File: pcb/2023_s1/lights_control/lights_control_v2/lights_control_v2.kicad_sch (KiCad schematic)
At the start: 9 parts

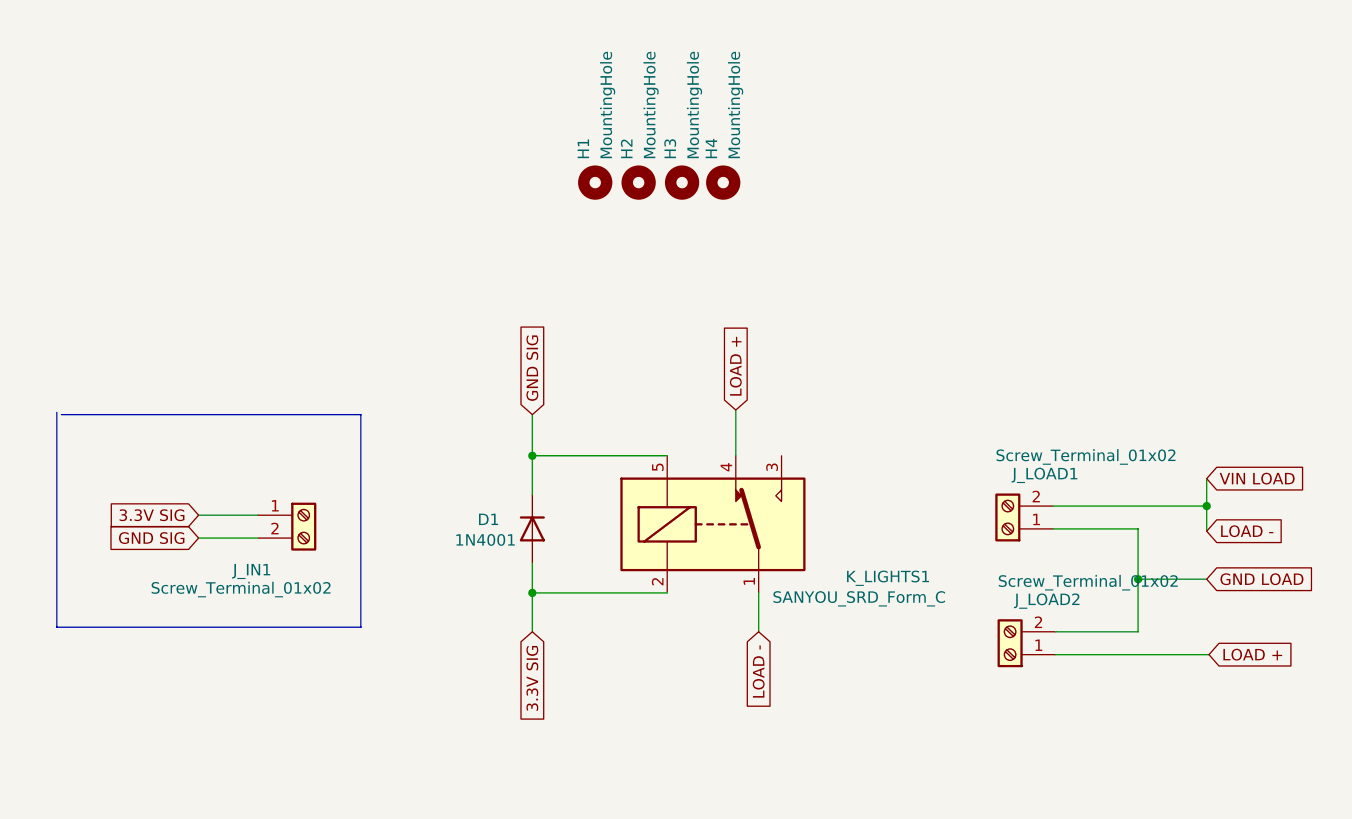
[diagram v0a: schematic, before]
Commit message: fix, forgot to use 2N2222 as current amplifier of the input signal
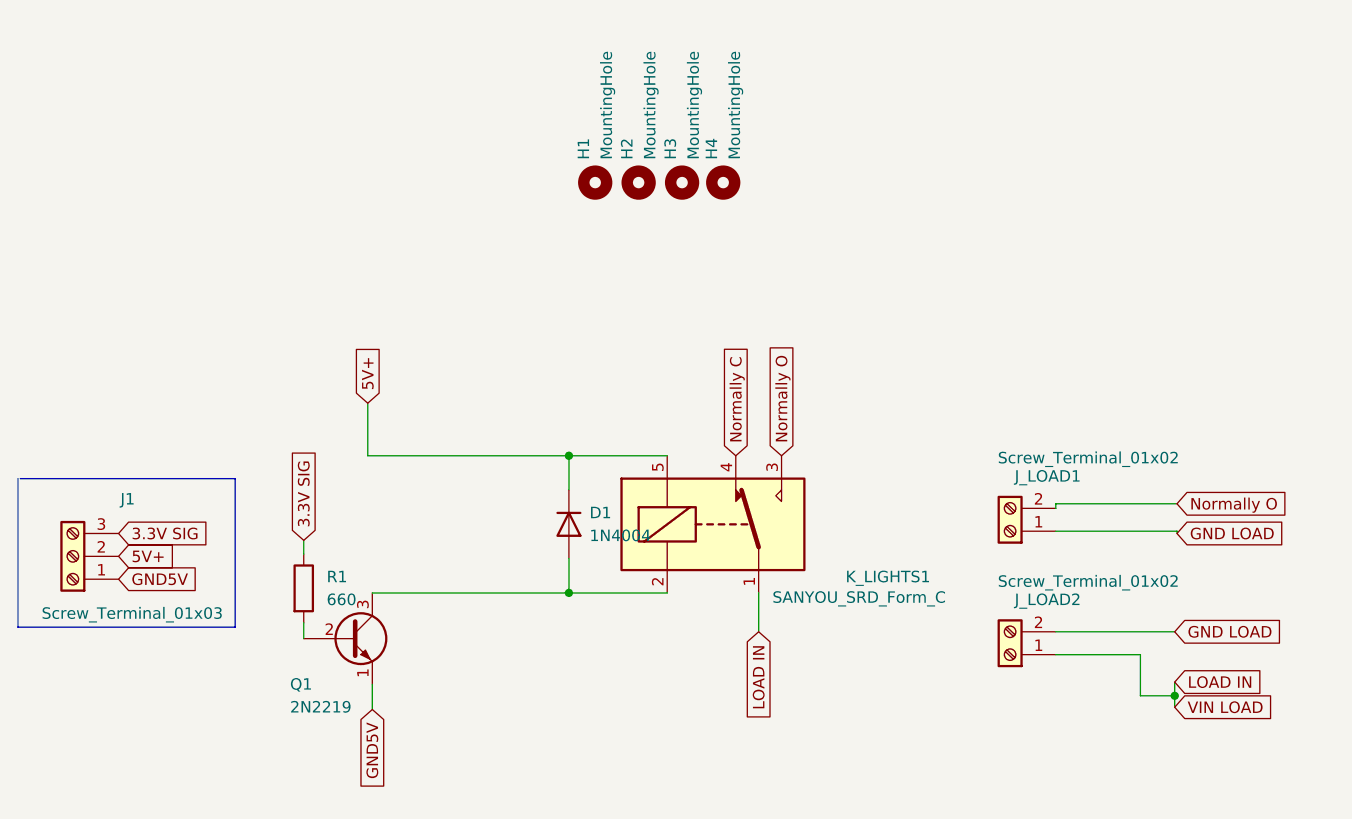
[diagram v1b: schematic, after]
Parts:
- removed D1: 1N4001, Diode_THT:D_DO-41_SOD81_P10.16mm_Horizontal, symbol Diode:1N4001
- removed J_IN1: Screw_Terminal_01x02, TerminalBlock:TerminalBlock_Altech_AK300-2_P5.00mm, symbol Connector:Screw_Terminal_01x02
- added D1: 1N4004, Diode_THT:D_DO-41_SOD81_P10.16mm_Horizontal, symbol Diode:1N4004
- added J1: Screw_Terminal_01x03, TerminalBlock:TerminalBlock_Altech_AK300-3_P5.00mm, symbol Connector:Screw_Terminal_01x03
- added Q1: 2N2219, Package_TO_SOT_THT:TO-39-3, symbol Transistor_BJT:2N2219
- added R1: 660, Resistor_THT:R_Axial_DIN0204_L3.6mm_D1.6mm_P2.54mm_Vertical, symbol Device:R
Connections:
- net 3.3V SIG: now also J1.3 (Pin_3), R1.1; no longer K_LIGHTS1.2
- net Normally O: now reaches K_LIGHTS1.3
- net Normally O: now also J_LOAD1.2 (Pin_2)
- net GND SIG renamed 5V+
- net 5V+: now also D1.1 (K), J1.2 (Pin_2)
- net LOAD + renamed LOAD IN
- net LOAD IN: now also K_LIGHTS1.1; no longer K_LIGHTS1.4
- removed net LOAD -: J_LOAD1.2 (Pin_2), K_LIGHTS1.1
- new net: D1.2 (A), K_LIGHTS1.2, Q1.3 (C)
- new net: Q1.2 (B), R1.2
- new net GND5V: J1.1 (Pin_1), Q1.1 (E)
- new net Normally C: K_LIGHTS1.4

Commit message: update
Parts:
- added R2: 50, Resistor_THT:R_Axial_DIN0204_L3.6mm_D1.6mm_P2.54mm_Vertical, symbol Device:R
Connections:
- net 5V+: now also R2.1; no longer D1.1 (K), K_LIGHTS1.5
- new net: D1.1 (K), K_LIGHTS1.5, R2.2
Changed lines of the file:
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@@
+    (stroke (width 0) (type default) (color 0 0 0 0))
+  )
+  (wire (pts (xy 121.412 82.296) (xy 121.412 84.328))
     (stroke (width 0) (type default) (color 0 0 0 0))
   )
@@
     (stroke (width 0) (type default) (color 0 0 0 0))
   )
+  (wire (pts (xy 121.412 84.328) (xy 128.524 84.328))
+    (stroke (width 0) (type default) (color 0 0 0 0))
+  )
   (wire (pts (xy 106.68 99.568) (xy 128.524 99.568))
     (stroke (width 0) (type default) (color 0 0 0 0))
   )
-  (wire (pts (xy 106.172 78.486) (xy 106.172 84.328))
+  (wire (pts (xy 121.412 71.628) (xy 121.412 74.676))
     (stroke (width 0) (type default) (color 0 0 0 0))
   )
@@
   )
   (wire (pts (xy 195.834 109.474) (xy 195.834 110.998))
-    (stroke (width 0) (type default) (color 0 0 0 0))
-  )
-  (wire (pts (xy 106.172 84.328) (xy 128.524 84.328))
     (stroke (width 0) (type default) (color 0 0 0 0))
   )
@@
     )
   )
-  (global_label "5V+" (shape input) (at 106.172 78.486 90) (fields_autoplaced)
-    (effects (font (size 1.27 1.27)) (justify left))
-    (property "Intersheet References" "${INTERSHEET_REFS}" (id 0) (at 106.2514 72.2024 90)
+  (global_label "5V+" (shape input) (at 121.412 71.628 90) (fields_autoplaced)
+    (effects (font (size 1.27 1.27)) (justify left))
+    (property "Intersheet References" "${INTERSHEET_REFS}" (id 0) (at 121.4914 65.3444 90)
       (effects (font (size 1.27 1.27)) (justify left) hide)
     )
@@
     (pin "2")
   )
+  (symbol (lib_id "Device:R") (at 121.412 78.486 0) (unit 1)
+    (in_bom yes) (on_board yes) (fields_autoplaced)
+    (property "Reference" "R2" (id 0) (at 123.19 77.2159 0)
+      (effects (font (size 1.27 1.27)) (justify left))
+    )
+    (property "Value" "50" (id 1) (at 123.19 79.7559 0)
+      (effects (font (size 1.27 1.27)) (justify left))
+    )
+    (property "Footprint" "Resistor_THT:R_Axial_DIN0204_L3.6mm_D1.6mm_P2.54mm_Vertical" (id 2) (at 119.634 78.486 90)
+      (effects (font (size 1.27 1.27)) hide)
+    )
+    (property "Datasheet" "~" (id 3) (at 121.412 78.486 0)
+      (effects (font (size 1.27 1.27)) hide)
+    )
+    (pin "1")
+    (pin "2")
+  )
   (symbol (lib_id "Mechanical:MountingHole") (at 145.669 53.975 90) (unit 1)
     (in_bom yes) (on_board yes)
@@
       (reference "R1") (unit 1) (value "660") (footprint "Resistor_THT:R_Axial_DIN0204_L3.6mm_D1.6mm_P2.54mm_Vertical")
     )
-  )
+    (path "/30d3c9fc-f51d-4e69-b4fa-a3bb1d23db9f"
+      (reference "R2") (unit 1) (value "50") (footprint "Resistor_THT:R_Axial_DIN0204_L3.6mm_D1.6mm_P2.54mm_Vertical")
+    )
+  )
